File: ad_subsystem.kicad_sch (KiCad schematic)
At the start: 5 parts, among them U2 ADS7886xxDBV, U3 CD4051B, U6 AD8603

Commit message: try to figure out how to do buses
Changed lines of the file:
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@@
+		)
+	)
+	(bus
+		(pts
+			(xy 57.15 59.69) (xy 72.39 59.69)
+		)
+		(stroke
+			(width 0)
+			(type default)
 		)
 	)
@@
 	(bus
 		(pts
-			(xy 58.42 59.69) (xy 57.15 59.69)
+			(xy 57.15 88.9) (xy 57.15 96.52)
 		)
 		(stroke
@@
 			(width 0)
 			(type default)
+		)
+	)
+	(label "{ad_ch}"
+		(at 59.69 59.69 0)
+		(effects
+			(font
+				(size 1.27 1.27)
+			)
+			(justify left bottom)
 		)
 	)
@@
 		)
 	)
-	(hierarchical_label "admux_CH"
+	(hierarchical_label "{ad_ch}"
 		(shape input)
-		(at 58.42 59.69 0)
-		(effects
-			(font
+		(at 72.39 59.69 0)
+		(effects
+			(font

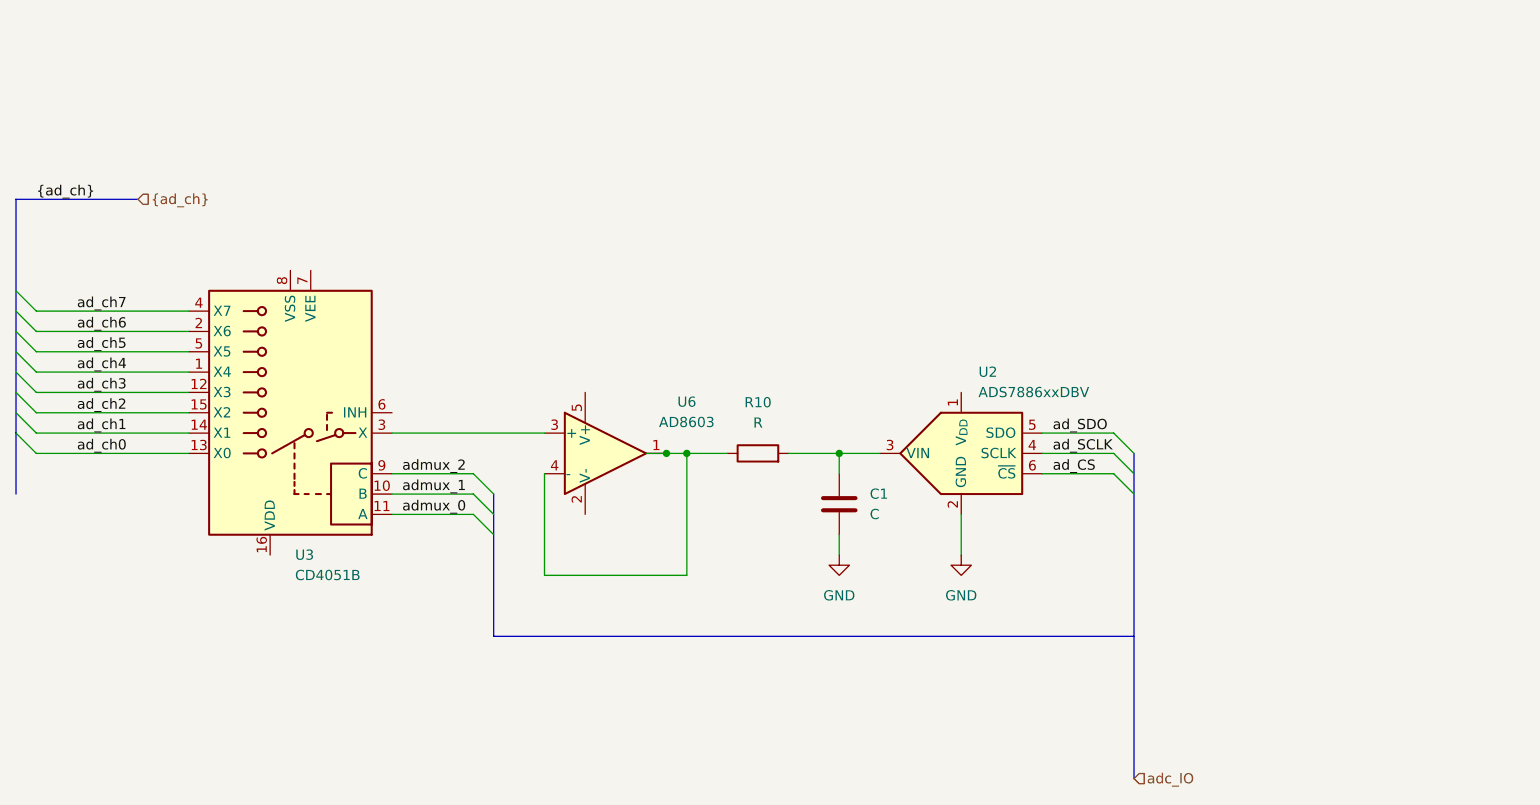
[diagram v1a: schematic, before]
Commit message: start adding power supplies
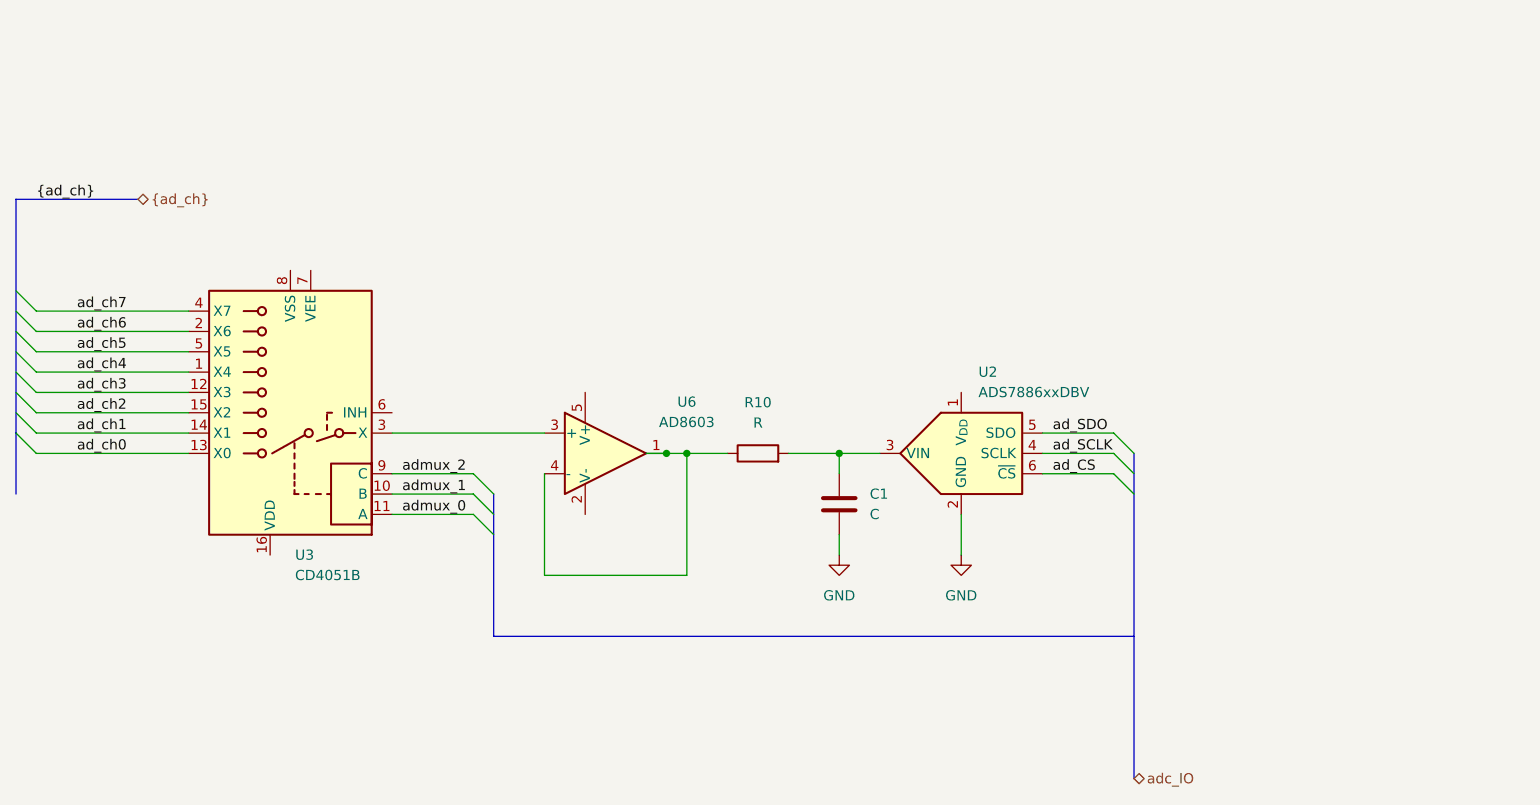
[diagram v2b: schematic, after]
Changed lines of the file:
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@@
 	)
 	(hierarchical_label "{ad_ch}"
-		(shape input)
+		(shape bidirectional)
 		(at 72.39 59.69 0)
 		(effects
@@
 	)
 	(hierarchical_label "adc_IO"
-		(shape input)
+		(shape bidirectional)
 		(at 196.85 132.08 0)
 		(effects

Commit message: add ads7056 footprint
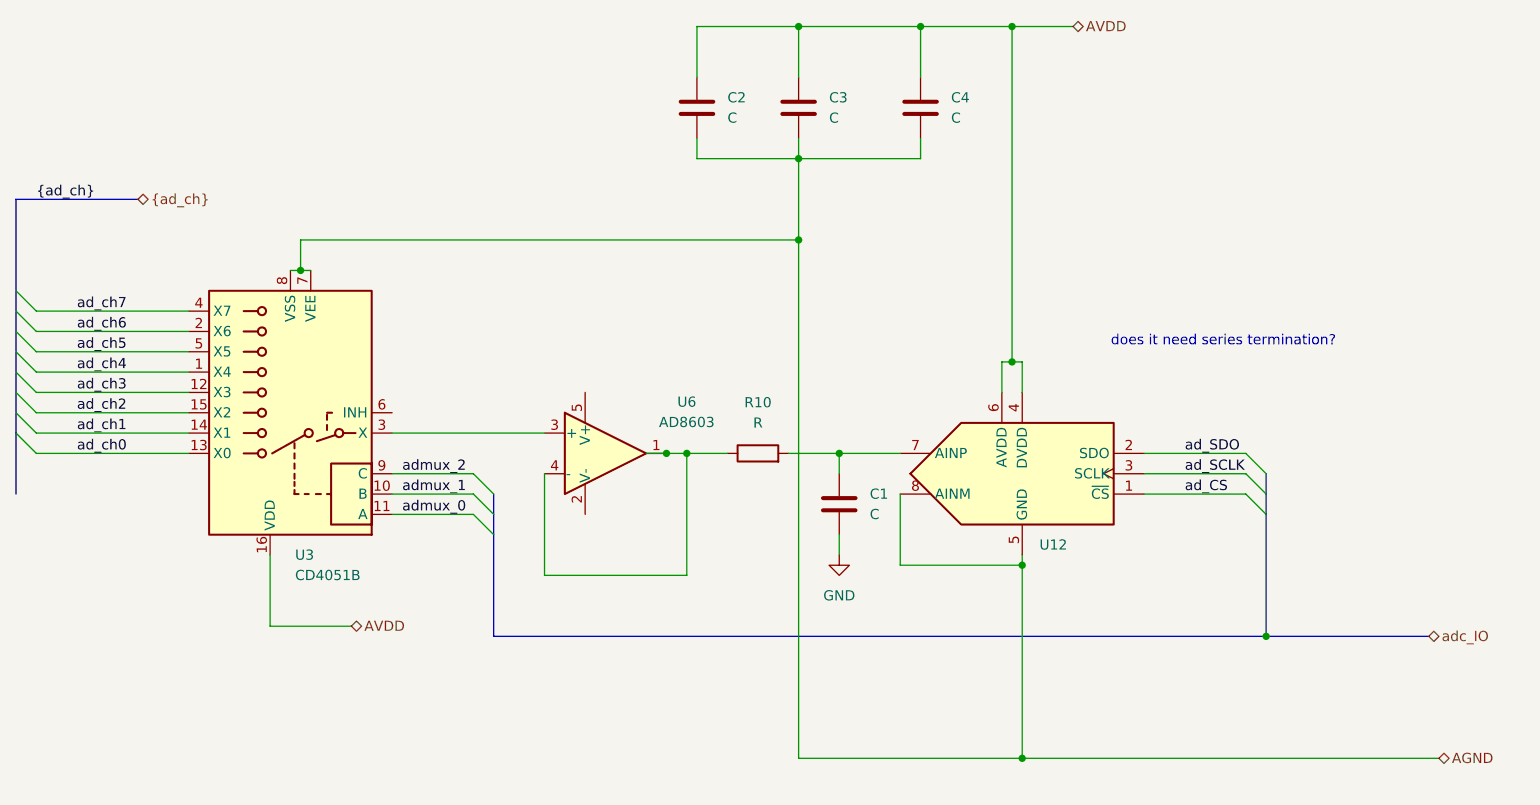
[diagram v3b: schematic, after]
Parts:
- removed U2: ADS7886xxDBV, Package_TO_SOT_SMD:SOT-23-6, symbol Analog_ADC:ADS7886xxDBV
- added C2, C3, C4: C, Capacitor_SMD:C_0402_1005Metric, symbol Device:C
- added U12: (no value), agilex_lib:ads7056, symbol agilex_5_lib:ADS7056
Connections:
- net ad_CS: now also U12.1 (~{CS})
- net ad_SCLK: now also U12.3 (SCLK)
- net ad_SDO: now also U12.2 (SDO)
- net at C1.1, R10.2: now also U12.7 (AINP)
- net AVDD: now reaches U3.16 (VDD)
- net AVDD: now also C2.1, C3.1, C4.1, U12.4 (DVDD), U12.6 (AVDD)
- net AGND: now reaches U3.7 (VEE)
- net AGND: now also U3.8 (VSS), C2.2, C3.2, C4.2, U12.5 (GND), U12.8 (AINM)
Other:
- note added: "does it need series termination?"

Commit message: start routing sd card
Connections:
- net AVDD: now also U3.6 (INH)

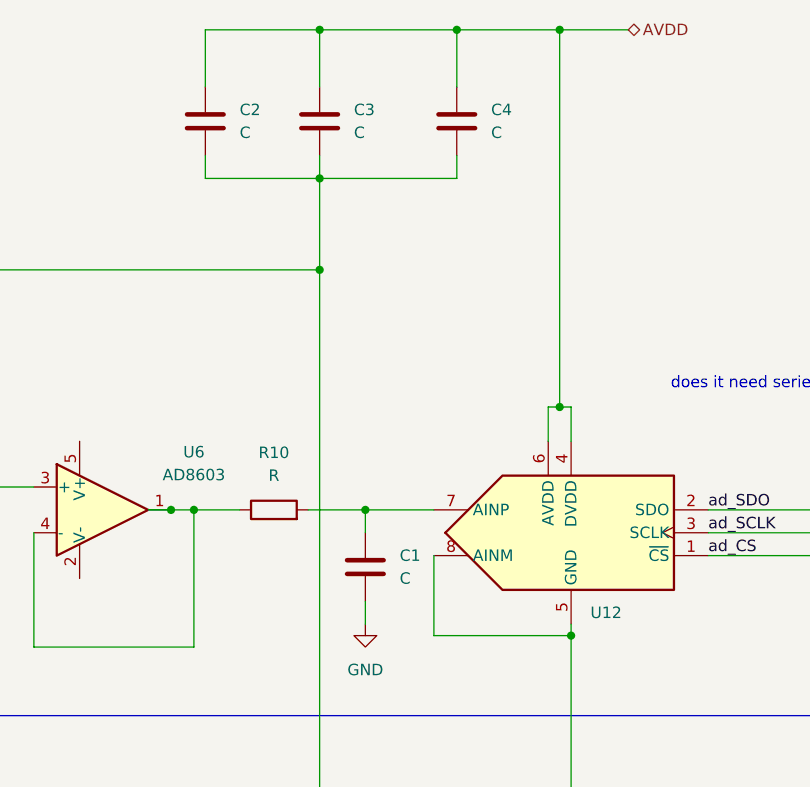
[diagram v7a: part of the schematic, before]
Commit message: add vias to lppdr balls
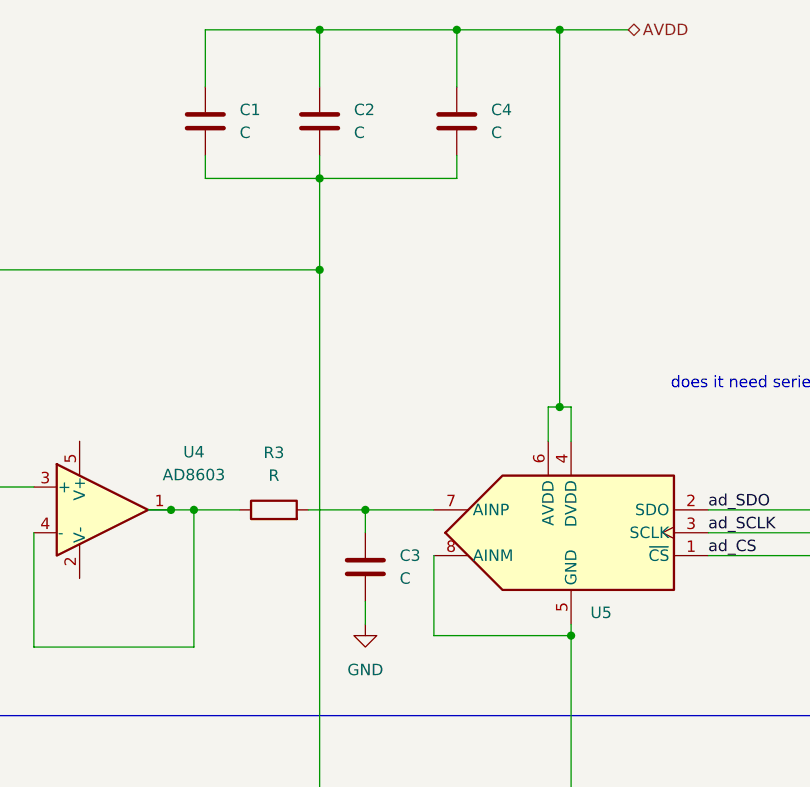
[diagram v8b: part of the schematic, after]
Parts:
- renumbered C2 to C1, C3 to C2, C1 to C3, R10 to R3, U6 to U4, U12 to U5
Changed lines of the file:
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@@
 		(dnp no)
 		(fields_autoplaced yes)
-		(property "Reference" "U6"
+		(property "Reference" "U4"
 			(at 140.97 85.0198 0)
 			(show_name no)
@@
 			(project "agilex_3_soc"
 				(path "/a5b98d95-6877-4284-904f-d04e32723ae0/871a81f2-62c4-47fa-98d5-872580aa51c3"
-					(reference "U6")
+					(reference "U4")
 					(unit 1)
 				)
@@
 		(in_pos_files yes)
 		(dnp no)
-		(property "Reference" "#PWR011"
+		(property "Reference" "#PWR019"
 			(at 160.02 110.49 0)
 			(hide yes)
@@
 			(project "agilex_3_soc"
 				(path "/a5b98d95-6877-4284-904f-d04e32723ae0/871a81f2-62c4-47fa-98d5-872580aa51c3"
-					(reference "#PWR011")
+					(reference "#PWR019")
 					(unit 1)
 				)
@@
 		(dnp no)
 		(fields_autoplaced yes)
-		(property "Reference" "C1"
+		(property "Reference" "C3"
 			(at 163.83 96.5199 0)
 			(show_name no)
@@
 			(project "agilex_3_soc"
 				(path "/a5b98d95-6877-4284-904f-d04e32723ae0/871a81f2-62c4-47fa-98d5-872580aa51c3"
-					(reference "C1")
+					(reference "C3")
 					(unit 1)
 				)
@@
 		(dnp no)
 		(fields_autoplaced yes)
-		(property "Reference" "R10"
+		(property "Reference" "R3"
 			(at 149.86 85.09 90)
 			(show_name no)
@@
 			(project "agilex_3_soc"
 				(path "/a5b98d95-6877-4284-904f-d04e32723ae0/871a81f2-62c4-47fa-98d5-872580aa51c3"
-					(reference "R10")
+					(reference "R3")
 					(unit 1)
 				)
@@
 		(dnp no)
 		(fields_autoplaced yes)
-		(property "Reference" "C2"
+		(property "Reference" "C1"
 			(at 146.05 46.9899 0)
 			(show_name no)
@@
 			(project "agilex_3_soc"
 				(path "/a5b98d95-6877-4284-904f-d04e32723ae0/871a81f2-62c4-47fa-98d5-872580aa51c3"
-					(reference "C2")
+					(reference "C1")
 					(unit 1)
 				)
@@
 		(dnp no)
 		(fields_autoplaced yes)
-		(property "Reference" "U12"
+		(property "Reference" "U5"
 			(at 185.0233 102.87 0)
 			(show_name no)
@@
 			(project "agilex_3_soc"
 				(path "/a5b98d95-6877-4284-904f-d04e32723ae0/871a81f2-62c4-47fa-98d5-872580aa51c3"
-					(reference "U12")
+					(reference "U5")
 					(unit 1)
 				)
@@
 		(dnp no)
 		(fields_autoplaced yes)
-		(property "Reference" "C3"
+		(property "Reference" "C2"
 			(at 158.75 46.9899 0)
 			(show_name no)
@@
 			(project "agilex_3_soc"
 				(path "/a5b98d95-6877-4284-904f-d04e32723ae0/871a81f2-62c4-47fa-98d5-872580aa51c3"
-					(reference "C3")
-					(unit 1)
-				)
+					(reference "C2")
+					(unit 1)
+				)
